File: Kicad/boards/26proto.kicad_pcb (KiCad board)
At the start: 2 copper layers, 84 x 61.5 mm, 35 parts, among them J1 5051104096, J10 Conn_01x05, J2 Micro_SD_Card, J3 URM37, J4 RE12A, J5 RS485_TFT, J6 RS485_airdata, J7 RS485_logger_2, J8 RS485_logger, J9 BNO085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

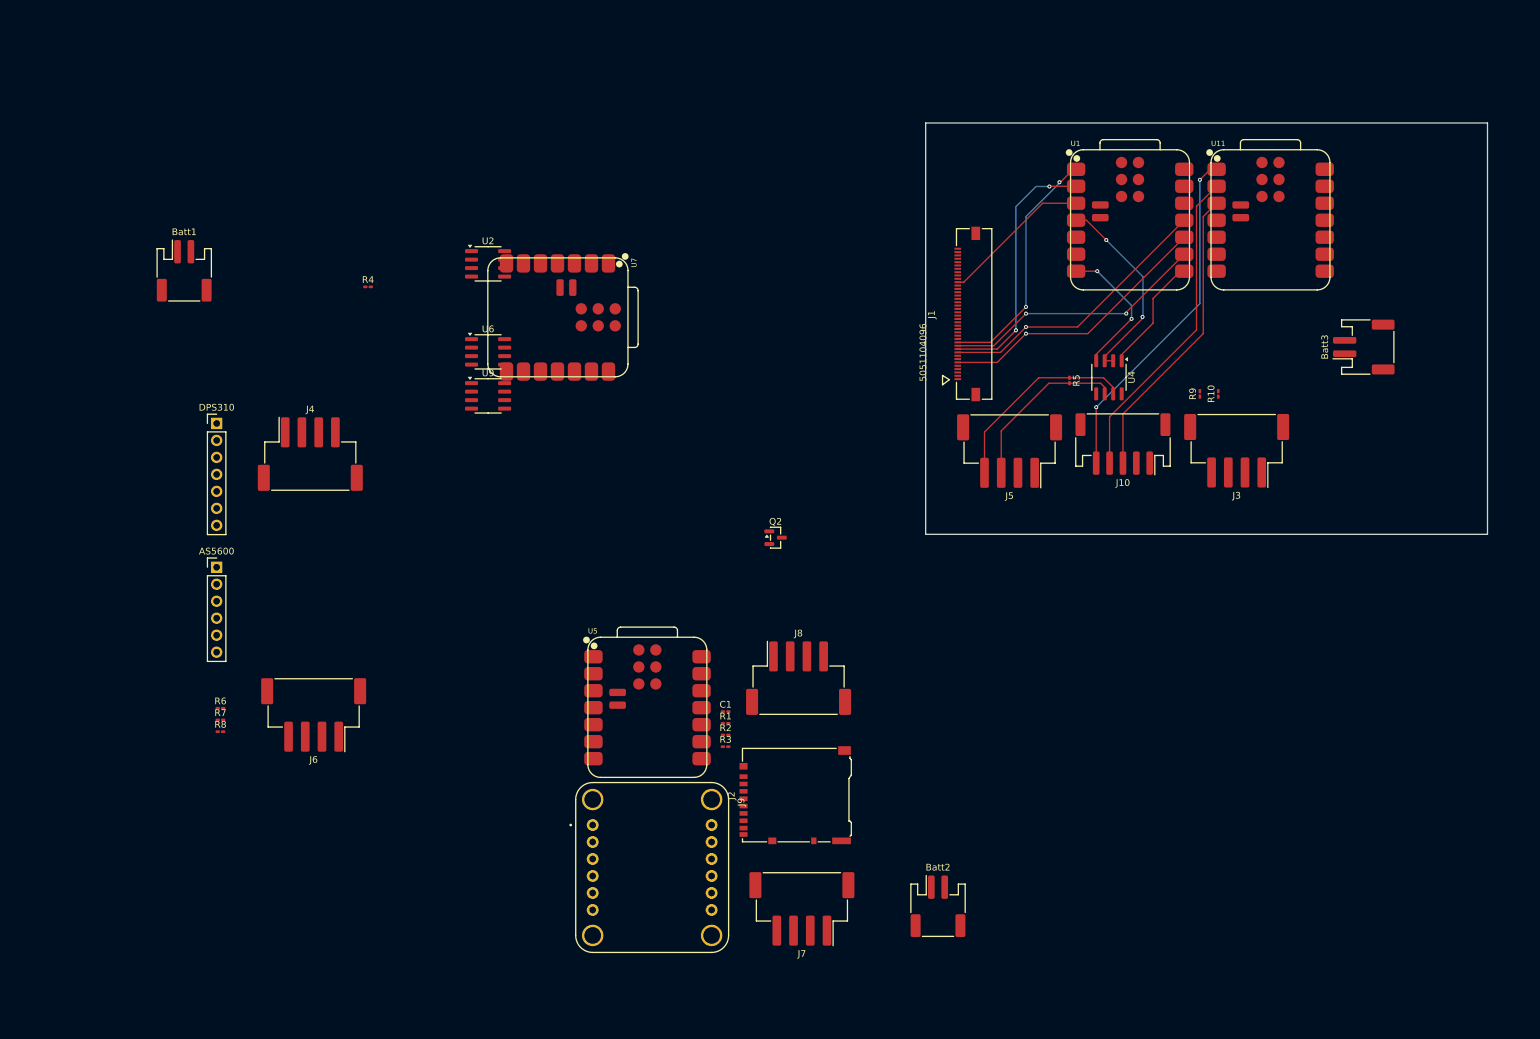
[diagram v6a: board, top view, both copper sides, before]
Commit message: added I2C wires
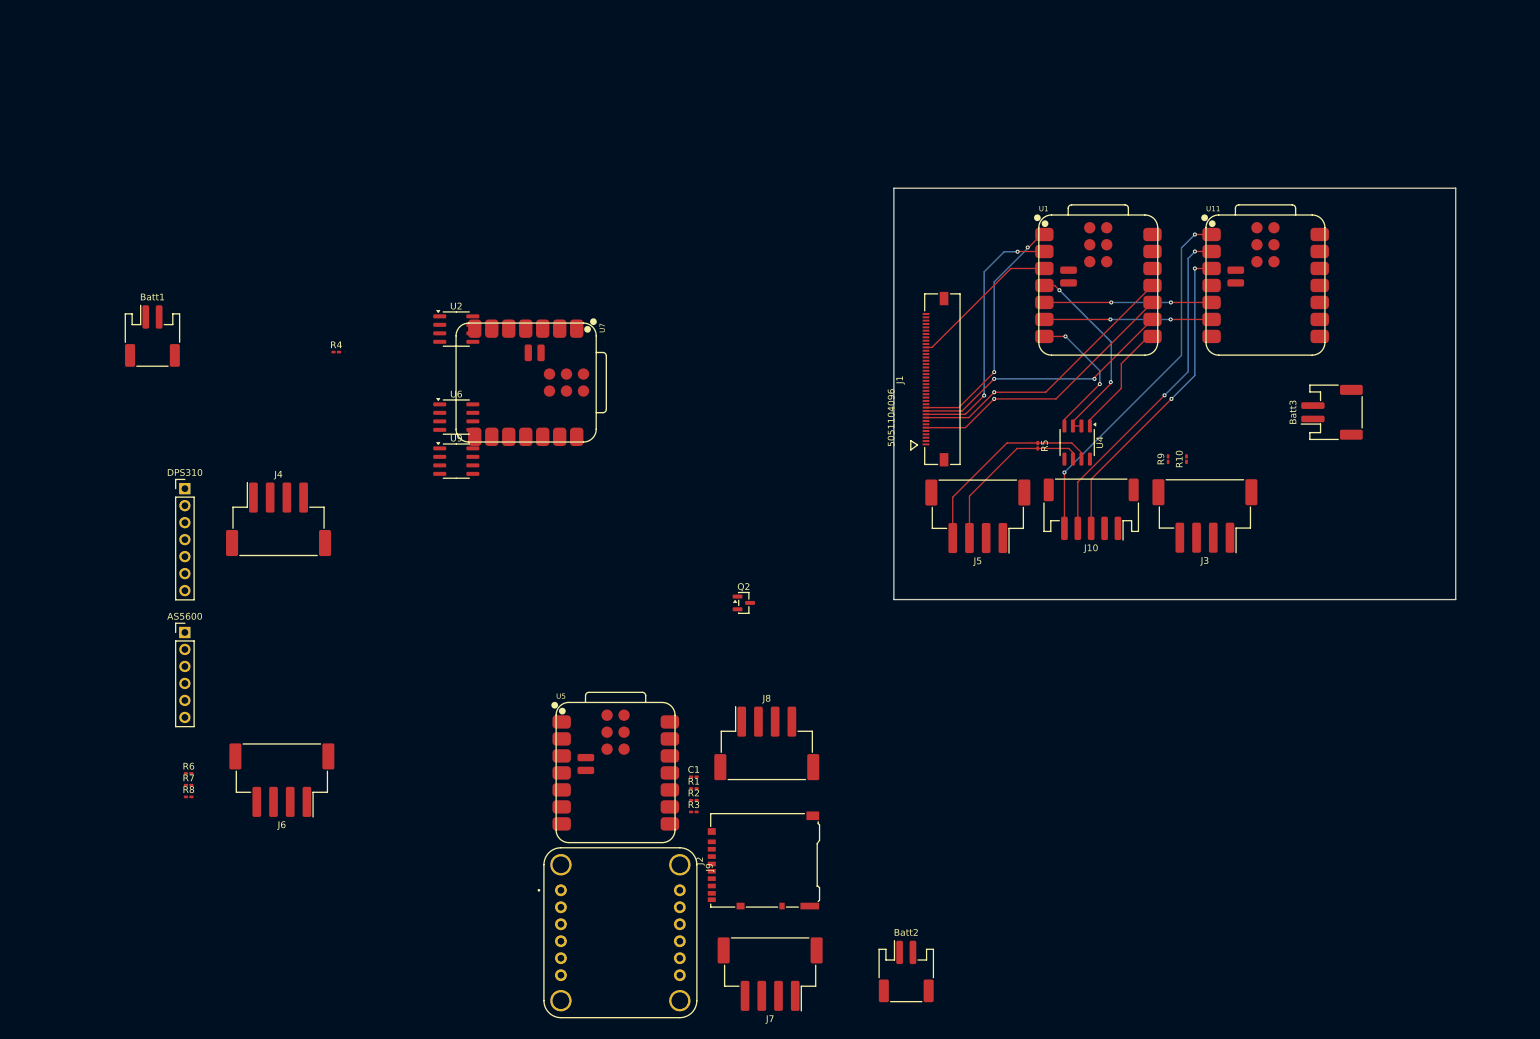
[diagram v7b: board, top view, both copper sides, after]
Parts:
- moved Batt2 10.8 mm to (146.1, 143.9)
- moved J7 10.8 mm to (125.8, 144.3)
- moved J5 10.8 mm to (156.8, 75.8)
- moved J1 10.8 mm to (151.5, 55.3)
- moved U4 10.8 mm to (171.7, 64.8)
- moved AS5600 10.8 mm to (38.3, 93.2)
- moved Batt1 10.8 mm to (33.4, 48.9)
- moved DPS310 10.8 mm to (38.3, 71.7)
- moved J4 10.8 mm to (52.3, 76.3)
- moved J6 10.8 mm to (52.8, 115.3)
- moved R6 10.8 mm to (38.8, 114.3)
- moved R7 10.8 mm to (38.8, 116.0)
- moved R8 10.8 mm to (38.8, 117.8)
- moved Batt3 10.8 mm to (209.8, 60.3)
- moved C1 10.8 mm to (114.3, 114.8)
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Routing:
- net SDA_board3: track 0.00 -> 25.0 mm, vias 0 -> 2
- net SCL_board3: track 0.00 -> 25.0 mm, vias 0 -> 2
- net Pot_rud: track 48.0 -> 51.2 mm, vias 0 -> 2
- net Pot_elv: track 44.6 -> 47.8 mm, vias 0 -> 2
- net Pot_trim: track 51.9 -> 54.5 mm

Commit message: updated logger and IMU board
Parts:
- added R11: R, Resistor_SMD:R_0201_0603Metric_Pad0.64x0.40mm_HandSolder, F.Cu at (188.1, 43.0)
- added R12: R, Resistor_SMD:R_0201_0603Metric_Pad0.64x0.40mm_HandSolder, F.Cu at (188.1, 45.5)
- added R13: R, Resistor_SMD:R_0201_0603Metric_Pad0.64x0.40mm_HandSolder, F.Cu at (194.5, 99.5)
- Batt2, Batt3, J7, J8, U2: moved to B.Cu
- moved U2 92.2 mm to (158.0, 95.0)
- moved R2 87.3 mm to (199.6, 99.5)
- moved R1 84.4 mm to (197.0, 99.5)
- moved J7 83.4 mm to (196.3, 99.7), turned to 0 degrees
- moved R3 80.3 mm to (192.0, 99.5)
- moved J9 78.8 mm to (175.6, 106.7)
- moved C1 74.4 mm to (188.0, 104.5), turned to -90 degrees
- moved J2 74.1 mm to (197.0, 110.7), turned to 0 degrees
- moved U5 50.7 mm to (153.0, 108.5), turned to 180 degrees
- moved Batt2 47.4 mm to (147.2, 96.5), turned to 90 degrees
- moved J8 30.9 mm to (155.9, 113.6), turned to 180 degrees
- moved Batt3 18.9 mm to (200.0, 76.5), turned to 180 degrees
- moved R10 12.7 mm to (175.5, 69.5), turned to 180 degrees
- moved R9 10.2 mm to (177.6, 60.5), turned to 180 degrees
- moved J10 5.72 mm to (179.1, 76.8), turned to 0 degrees
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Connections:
- J3 pad 3: RX_URM37 -> TX_URM37
- J3 pad 4: TX_URM37 -> RX_URM37
- J9 pad JP1_1: (no net) -> +3.3V
- J9 pad JP1_2: (no net) -> unconnected-(J9-3VO-PadJP1_2)
- J9 pad JP1_3: (no net) -> encoder_cathode
- J9 pad JP1_4: (no net) -> SCL_BNO085
- J9 pad JP1_5: (no net) -> SDA_BNO085
- J9 pad JP1_6: (no net) -> unconnected-(J9-~{INT}-PadJP1_6)
- J9 pad JP2_1: (no net) -> unconnected-(J9-BT-PadJP2_1)
- J9 pad JP2_2: (no net) -> unconnected-(J9-P0-PadJP2_2)
- J9 pad JP2_3: (no net) -> unconnected-(J9-P1-PadJP2_3)
- J9 pad JP2_4: (no net) -> unconnected-(J9-~{RST}-PadJP2_4)
- J9 pad JP2_5: (no net) -> unconnected-(J9-DI-PadJP2_5)
- J9 pad JP2_6: (no net) -> unconnected-(J9-CS-PadJP2_6)
- U11 pad 1: Pot_trim -> Pot_elv
- U11 pad 3: Pot_elv -> Pot_trim
- U5 pad 1: CS_SD -> Net-(U2-DE)
- U5 pad 4: Net-(U2-DE) -> CS_SD
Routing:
- net +BATT: track 0.00 -> 97.6 mm, vias 0 -> 5
- net +3.3V: track 0.00 -> 77.1 mm
- net SCLK_SD: track 0.00 -> 54.3 mm
- net MOSI_SD: track 0.00 -> 52.9 mm
- net MISO_SD: track 0.00 -> 52.3 mm
- net CS_SD: track 0.00 -> 44.9 mm
- net RX_URM37: track 0.00 -> 31.4 mm
- net Net-(U2-DE): track 0.00 -> 27.1 mm, vias 0 -> 1
- net TX_URM37: track 0.00 -> 25.4 mm
- net RS485_B: track 30.3 -> 11.2 mm
- net Pot_trim: track 54.5 -> 41.1 mm
- net RS485_A: track 25.9 -> 12.7 mm
- net encoder_cathode: track 0.00 -> 8.98 mm, vias 0 -> 2
- net SCL_BNO085: track 0.00 -> 7.60 mm
- net SDA_BNO085: track 0.00 -> 7.60 mm
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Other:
- board size 84 x 61.5 mm -> 73.1 x 89.4 mm
